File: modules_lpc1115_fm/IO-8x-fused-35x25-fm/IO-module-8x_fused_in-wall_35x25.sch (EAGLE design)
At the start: 82 parts, among them IC1 LPC1115, IC2 ATAES132A-SHEQ-T, Q2 ASFL, U1 EEPROM, X3 MICROMATCH-10

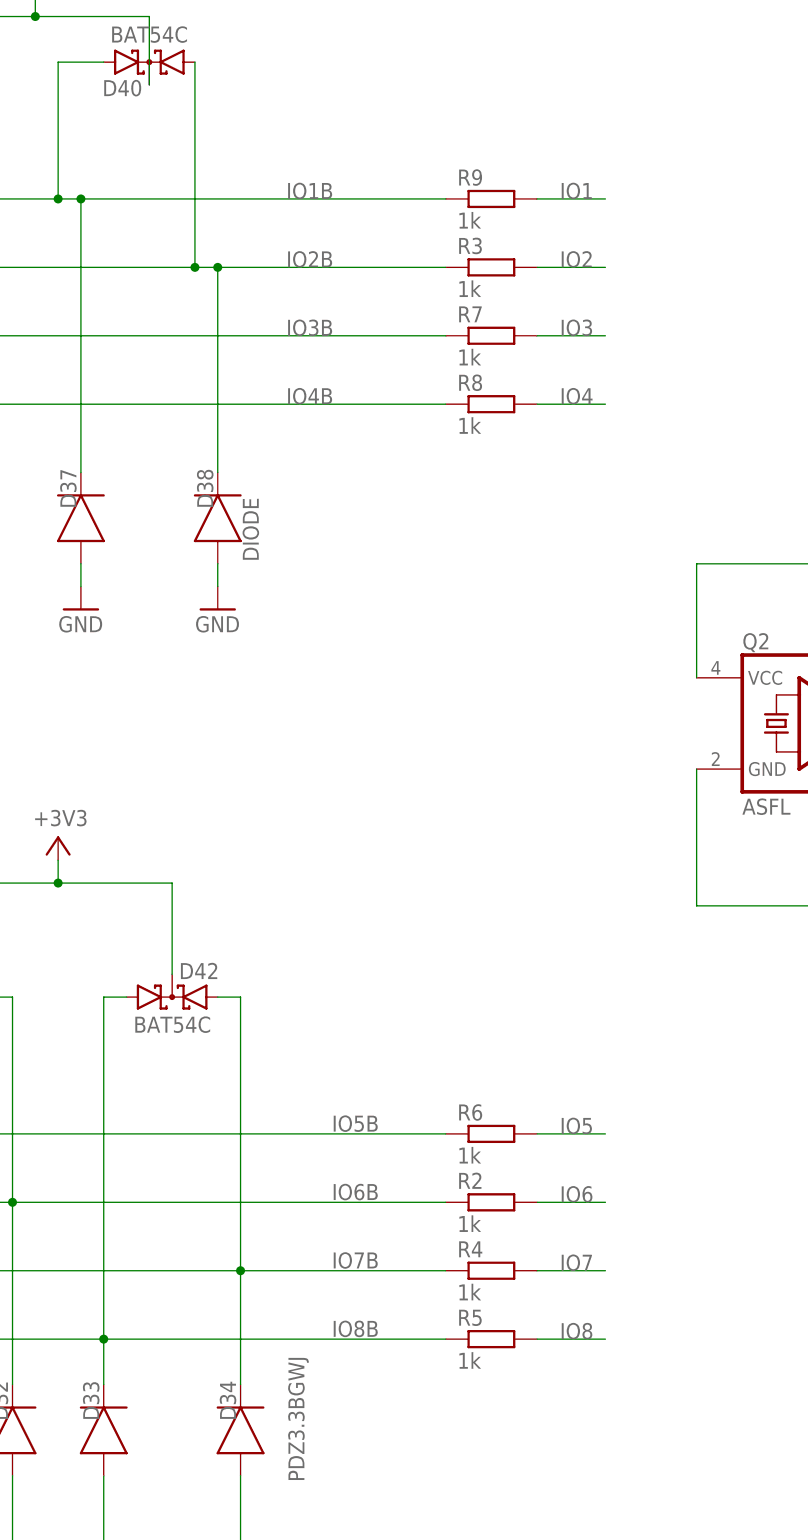
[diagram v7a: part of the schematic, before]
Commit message: [IOmodule8xUP] added values of 100R resistors; optimized routing
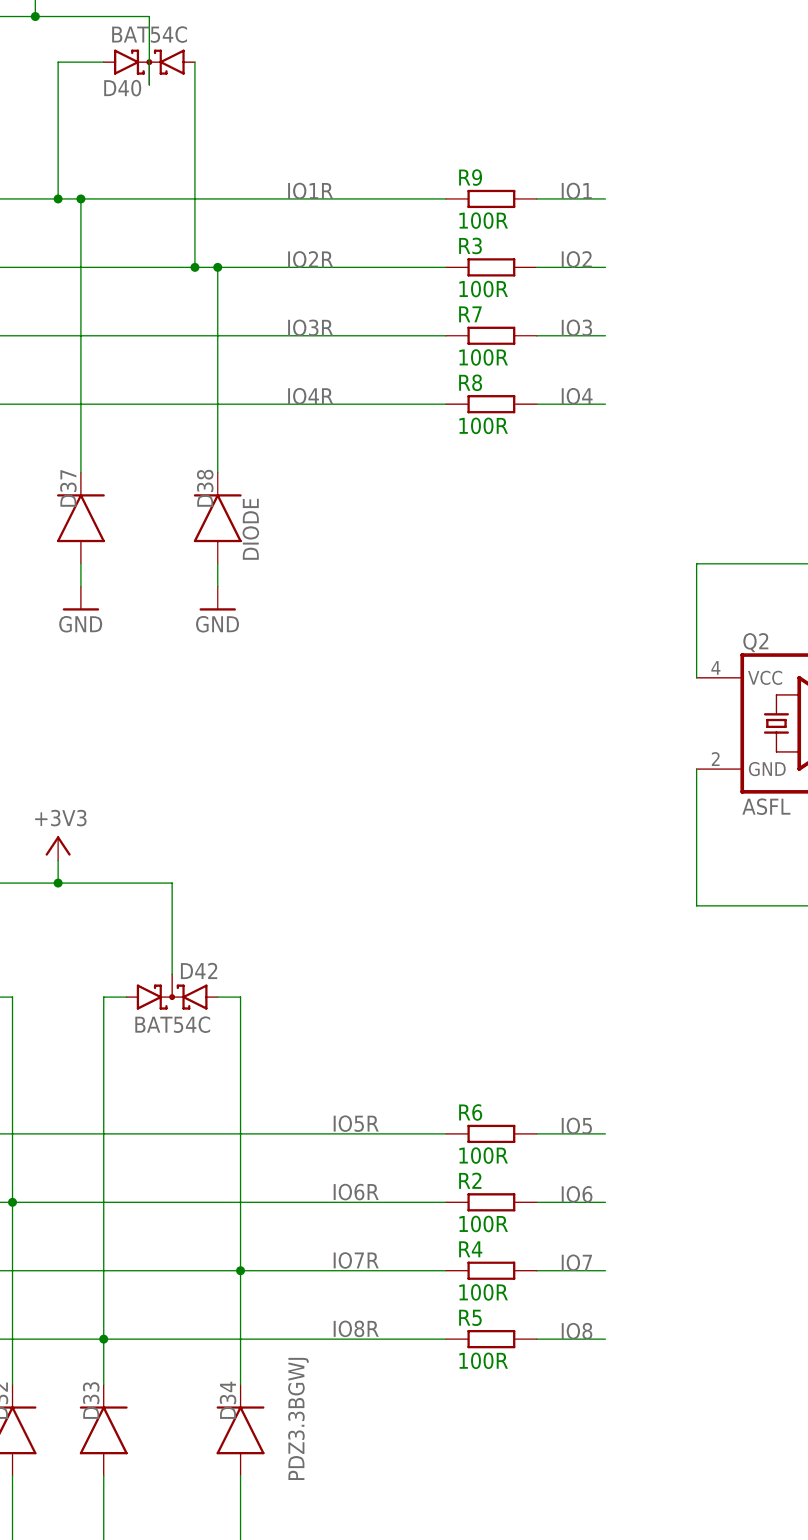
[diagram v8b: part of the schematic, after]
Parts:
- R2, R3, R4, R5, R6, R7, R8, R9: value 1k -> 100R
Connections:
- net IO1B renamed IO1R
- net IO2B renamed IO2R
- net IO3B renamed IO3R
- net IO4B renamed IO4R
- net IO5B renamed IO5R
- net IO6B renamed IO6R
- net IO7B renamed IO7R
- net IO8B renamed IO8R
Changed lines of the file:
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@@
 <part name="GND3" library="supply1" deviceset="GND" device=""/>
 <part name="P+3" library="supply1" deviceset="+3V3" device=""/>
-<part name="R2" library="rcl" library_urn="urn:adsk.eagle:library:334" deviceset="R-EU_" device="R0805" package3d_urn="urn:adsk.eagle:package:23553/2" value="1k"/>
-<part name="R4" library="rcl" library_urn="urn:adsk.eagle:library:334" deviceset="R-EU_" device="R0805" package3d_urn="urn:adsk.eagle:package:23553/2" value="1k"/>
-<part name="R5" library="rcl" library_urn="urn:adsk.eagle:library:334" deviceset="R-EU_" device="R0805" package3d_urn="urn:adsk.eagle:package:23553/2" value="1k"/>
-<part name="R6" library="rcl" library_urn="urn:adsk.eagle:library:334" deviceset="R-EU_" device="R0805" package3d_urn="urn:adsk.eagle:package:23553/2" value="1k"/>
-<part name="R3" library="rcl" library_urn="urn:adsk.eagle:library:334" deviceset="R-EU_" device="R0805" package3d_urn="urn:adsk.eagle:package:23553/2" value="1k"/>
-<part name="R7" library="rcl" library_urn="urn:adsk.eagle:library:334" deviceset="R-EU_" device="R0805" package3d_urn="urn:adsk.eagle:package:23553/2" value="1k"/>
-<part name="R8" library="rcl" library_urn="urn:adsk.eagle:library:334" deviceset="R-EU_" device="R0805" package3d_urn="urn:adsk.eagle:package:23553/2" value="1k"/>
-<part name="R9" library="rcl" library_urn="urn:adsk.eagle:library:334" deviceset="R-EU_" device="R0805" package3d_urn="urn:adsk.eagle:package:23553/2" value="1k"/>
+<part name="R2" library="rcl" library_urn="urn:adsk.eagle:library:334" deviceset="R-EU_" device="R0805" package3d_urn="urn:adsk.eagle:package:23553/2" value="100R"/>
+<part name="R4" library="rcl" library_urn="urn:adsk.eagle:library:334" deviceset="R-EU_" device="R0805" package3d_urn="urn:adsk.eagle:package:23553/2" value="100R"/>
+<part name="R5" library="rcl" library_urn="urn:adsk.eagle:library:334" deviceset="R-EU_" device="R0805" package3d_urn="urn:adsk.eagle:package:23553/2" value="100R"/>
+<part name="R6" library="rcl" library_urn="urn:adsk.eagle:library:334" deviceset="R-EU_" device="R0805" package3d_urn="urn:adsk.eagle:package:23553/2" value="100R"/>
+<part name="R3" library="rcl" library_urn="urn:adsk.eagle:library:334" deviceset="R-EU_" device="R0805" package3d_urn="urn:adsk.eagle:package:23553/2" value="100R"/>
+<part name="R7" library="rcl" library_urn="urn:adsk.eagle:library:334" deviceset="R-EU_" device="R0805" package3d_urn="urn:adsk.eagle:package:23553/2" value="100R"/>
+<part name="R8" library="rcl" library_urn="urn:adsk.eagle:library:334" deviceset="R-EU_" device="R0805" package3d_urn="urn:adsk.eagle:package:23553/2" value="100R"/>
+<part name="R9" library="rcl" library_urn="urn:adsk.eagle:library:334" deviceset="R-EU_" device="R0805" package3d_urn="urn:adsk.eagle:package:23553/2" value="100R"/>
 </parts>
 <sheets>
@@
 </instance>
 <instance part="R2" gate="G$1" x="210.82" y="50.8" smashed="yes">
-<attribute name="NAME" x="207.01" y="52.2986" size="1.778" layer="95"/>
-<attribute name="VALUE" x="207.01" y="47.498" size="1.778" layer="96"/>
+<attribute name="NAME" x="207.01" y="52.2986" size="1.778" layer="91"/>
+<attribute name="VALUE" x="207.01" y="47.498" size="1.778" layer="91"/>
 </instance>
 <instance part="R4" gate="G$1" x="210.82" y="43.18" smashed="yes">
-<attribute name="NAME" x="207.01" y="44.6786" size="1.778" layer="95"/>
-<attribute name="VALUE" x="207.01" y="39.878" size="1.778" layer="96"/>
+<attribute name="NAME" x="207.01" y="44.6786" size="1.778" layer="91"/>
+<attribute name="VALUE" x="207.01" y="39.878" size="1.778" layer="91"/>
 </instance>
 <instance part="R5" gate="G$1" x="210.82" y="35.56" smashed="yes">
-<attribute name="NAME" x="207.01" y="37.0586" size="1.778" layer="95"/>
-<attribute name="VALUE" x="207.01" y="32.258" size="1.778" layer="96"/>
+<attribute name="NAME" x="207.01" y="37.0586" size="1.778" layer="91"/>
+<attribute name="VALUE" x="207.01" y="32.258" size="1.778" layer="91"/>
 </instance>
 <instance part="R6" gate="G$1" x="210.82" y="58.42" smashed="yes">
-<attribute name="NAME" x="207.01" y="59.9186" size="1.778" layer="95"/>
-<attribute name="VALUE" x="207.01" y="55.118" size="1.778" layer="96"/>
+<attribute name="NAME" x="207.01" y="59.9186" size="1.778" layer="91"/>
+<attribute name="VALUE" x="207.01" y="55.118" size="1.778" layer="91"/>
 </instance>
 <instance part="R3" gate="G$1" x="210.82" y="154.94" smashed="yes">
-<attribute name="NAME" x="207.01" y="156.4386" size="1.778" layer="95"/>
-<attribute name="VALUE" x="207.01" y="151.638" size="1.778" layer="96"/>
+<attribute name="NAME" x="207.01" y="156.4386" size="1.778" layer="91"/>
+<attribute name="VALUE" x="207.01" y="151.638" size="1.778" layer="91"/>
 </instance>
 <instance part="R7" gate="G$1" x="210.82" y="147.32" smashed="yes">
-<attribute name="NAME" x="207.01" y="148.8186" size="1.778" layer="95"/>
-<attribute name="VALUE" x="207.01" y="144.018" size="1.778" layer="96"/>
+<attribute name="NAME" x="207.01" y="148.8186" size="1.778" layer="91"/>
+<attribute name="VALUE" x="207.01" y="144.018" size="1.778" layer="91"/>
 </instance>
 <instance part="R8" gate="G$1" x="210.82" y="139.7" smashed="yes">
-<attribute name="NAME" x="207.01" y="141.1986" size="1.778" layer="95"/>
-<attribute name="VALUE" x="207.01" y="136.398" size="1.778" layer="96"/>
+<attribute name="NAME" x="207.01" y="141.1986" size="1.778" layer="91"/>
+<attribute name="VALUE" x="207.01" y="136.398" size="1.778" layer="91"/>
 </instance>
 <instance part="R9" gate="G$1" x="210.82" y="162.56" smashed="yes">
-<attribute name="NAME" x="207.01" y="164.0586" size="1.778" layer="95"/>
-<attribute name="VALUE" x="207.01" y="159.258" size="1.778" layer="96"/>
+<attribute name="NAME" x="207.01" y="164.0586" size="1.778" layer="91"/>
+<attribute name="VALUE" x="207.01" y="159.258" size="1.778" layer="91"/>
 </instance>
 </instances>
@@
 <pinref part="R2" gate="G$1" pin="2"/>
 <wire x1="215.9" y1="50.8" x2="223.52" y2="50.8" width="0.1524" layer="91"/>
-<label x="218.44" y="50.8" size="1.778" layer="95"/>
+<label x="218.44" y="50.8" size="1.778" layer="91"/>
 </segment>
 </net>
@@
 <pinref part="R6" gate="G$1" pin="2"/>
 <wire x1="215.9" y1="58.42" x2="223.52" y2="58.42" width="0.1524" layer="91"/>
-<label x="218.44" y="58.42" size="1.778" layer="95"/>
+<label x="218.44" y="58.42" size="1.778" layer="91"/>
 </segment>
 </net>
@@
 <pinref part="R4" gate="G$1" pin="2"/>
 <wire x1="215.9" y1="43.18" x2="223.52" y2="43.18" width="0.1524" layer="91"/>
-<label x="218.44" y="43.18" size="1.778" layer="95"/>
+<label x="218.44" y="43.18" size="1.778" layer="91"/>
 </segment>
 </net>
@@
 <pinref part="R5" gate="G$1" pin="2"/>
 <wire x1="215.9" y1="35.56" x2="223.52" y2="35.56" width="0.1524" layer="91"/>
-<label x="218.44" y="35.56" size="1.778" layer="95"/>
+<label x="218.44" y="35.56" size="1.778" layer="91"/>
 </segment>
 </net>
@@
 <pinref part="R8" gate="G$1" pin="2"/>
 <wire x1="215.9" y1="139.7" x2="223.52" y2="139.7" width="0.1524" layer="91"/>
-<label x="218.44" y="139.7" size="1.778" layer="95"/>
+<label x="218.44" y="139.7" size="1.778" layer="91"/>
 </segment>
 </net>
@@
 <pinref part="R7" gate="G$1" pin="2"/>
 <wire x1="215.9" y1="147.32" x2="223.52" y2="147.32" width="0.1524" layer="91"/>
-<label x="218.44" y="147.32" size="1.778" layer="95"/>
+<label x="218.44" y="147.32" size="1.778" layer="91"/>
 </segment>
 </net>
@@
 <pinref part="R3" gate="G$1" pin="2"/>
 <wire x1="215.9" y1="154.94" x2="223.52" y2="154.94" width="0.1524" layer="91"/>
-<label x="218.44" y="154.94" size="1.778" layer="95"/>
+<label x="218.44" y="154.94" size="1.778" layer="91"/>
 </segment>
 </net>
@@
 <pinref part="R9" gate="G$1" pin="2"/>
 <wire x1="215.9" y1="162.56" x2="223.52" y2="162.56" width="0.1524" layer="91"/>
-<label x="218.44" y="162.56" size="1.778" layer="95"/>
+<label x="218.44" y="162.56" size="1.778" layer="91"/>
 </segment>
 </net>
@@
 </segment>
 </net>
-<net name="IO5B" class="0">
+<net name="IO5R" class="0">
 <segment>
 <wire x1="142.24" y1="58.42" x2="142.24" y2="30.48" width="0.1524" layer="91"/>
@@
 </segment>
 </net>
-<net name="IO6B" class="0">
+<net name="IO6R" class="0">
 <segment>
 <pinref part="D41" gate="G$1" pin="A2"/>
@@
 </segment>
 </net>
-<net name="IO7B" class="0">
+<net name="IO7R" class="0">
 <segment>
 <label x="193.04" y="43.434" size="1.778" layer="95"/>
@@
 </segment>
 </net>
-<net name="IO8B" class="0">
+<net name="IO8R" class="0">
 <segment>
 <label x="193.04" y="35.814" size="1.778" layer="95"/>
@@
 </segment>
 </net>
-<net name="IO1B" class="0">
+<net name="IO1R" class="0">
 <segment>
 <wire x1="165.1" y1="162.56" x2="165.1" y2="132.08" width="0.1524" layer="91"/>
@@
 </segment>
 </net>
-<net name="IO2B" class="0">
+<net name="IO2R" class="0">
 <segment>
 <wire x1="180.34" y1="154.94" x2="180.34" y2="132.08" width="0.1524" layer="91"/>
@@
 </segment>
 </net>
-<net name="IO3B" class="0">
+<net name="IO3R" class="0">
 <segment>
 <wire x1="137.16" y1="147.32" x2="137.16" y2="132.08" width="0.1524" layer="91"/>
@@
 </segment>
 </net>
-<net name="IO4B" class="0">
+<net name="IO4R" class="0">
 <segment>
 <wire x1="152.4" y1="139.7" x2="152.4" y2="132.08" width="0.1524" layer="91"/>
